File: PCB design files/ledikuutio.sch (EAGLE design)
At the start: 71 parts, among them IC1 ATMEGA328P, IC2 ISO7221A, IC3 74HC595D, Q2 MOSFET-NCHANNELSMD, Q3 16mhz, T1 TIP42, T2 TIP42, T3 TIP42, T4 TIP42, T5 TIP42, T6 TIP42, T7 TIP42, T8 TIP42, X1 2516-, X2 5566-20, X3 2516-, X4 2516-, X5 2516-, X6 2510-, X7 ANALOG IO

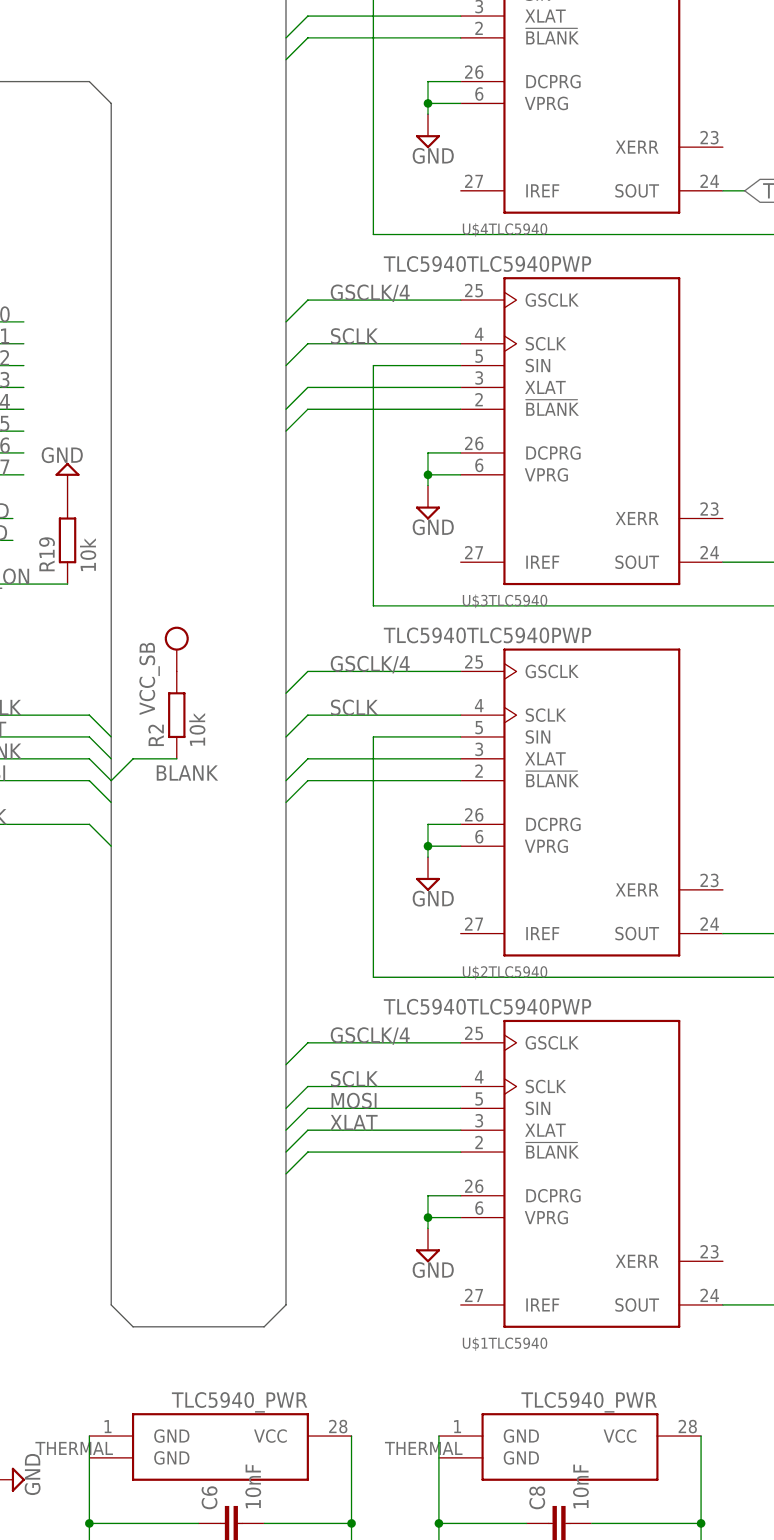
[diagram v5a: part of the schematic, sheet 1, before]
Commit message: Add missing IREF resistors.
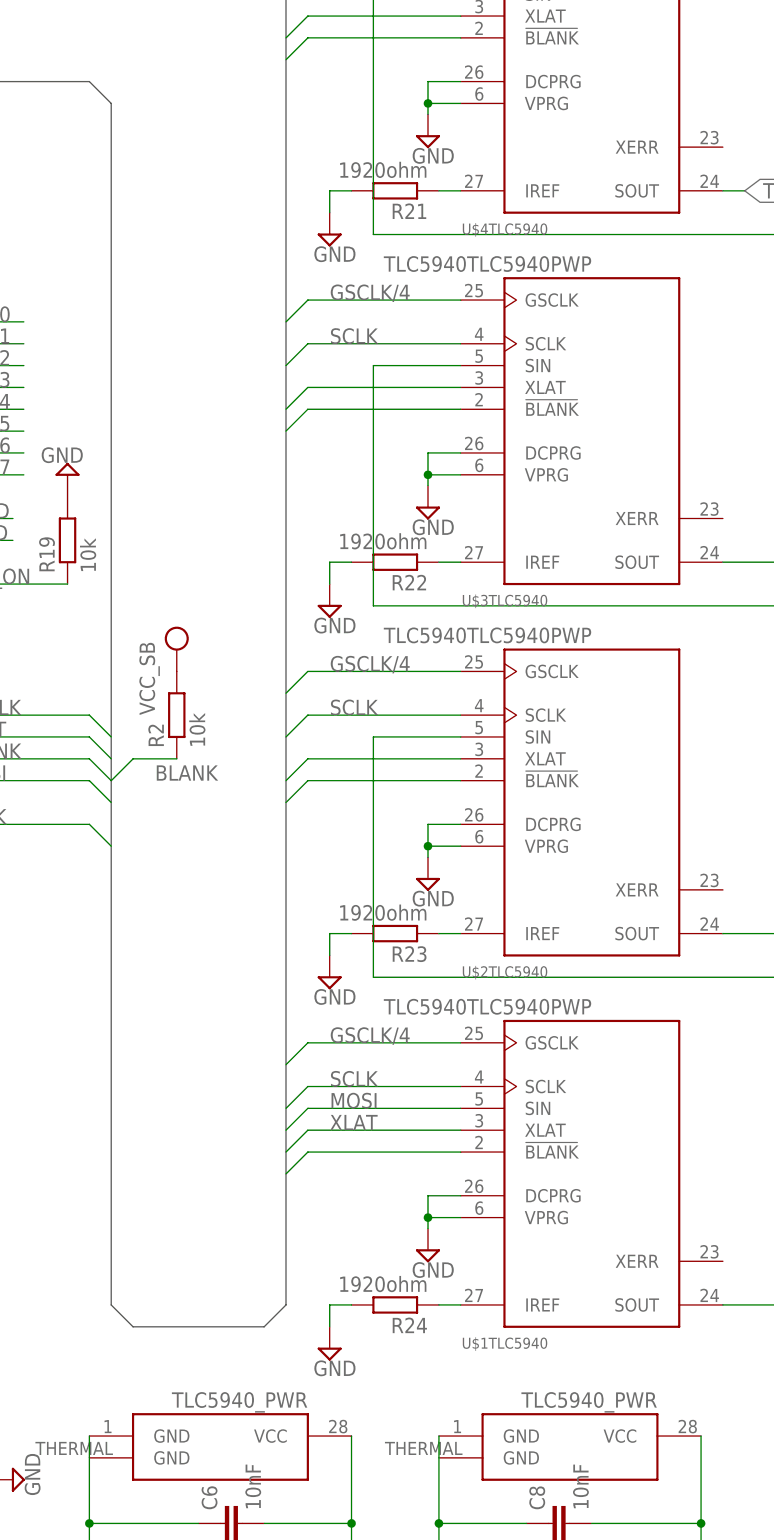
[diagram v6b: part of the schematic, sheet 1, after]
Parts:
- added R21, R22, R23, R24: 1920ohm, rcl:R-EU_M0805
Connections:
- new net N$48: R24.1, U$1TLC5940.IREF
- new net N$5: R21.1, U$4TLC5940.IREF
- new net N$6: R23.1, U$2TLC5940.IREF
- new net N$99: R22.1, U$3TLC5940.IREF
- net GND: now also R21.2, R22.2, R23.2, R24.2
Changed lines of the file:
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@@
 <part name="SUPPLY25" library="supply2" deviceset="GND" device=""/>
 <part name="R20" library="rcl" deviceset="R-EU_" device="M0805" value="10k"/>
+<part name="R21" library="rcl" deviceset="R-EU_" device="M0805" value="1920ohm"/>
+<part name="SUPPLY26" library="supply2" deviceset="GND" device=""/>
+<part name="R22" library="rcl" deviceset="R-EU_" device="M0805" value="1920ohm"/>
+<part name="R23" library="rcl" deviceset="R-EU_" device="M0805" value="1920ohm"/>
+<part name="R24" library="rcl" deviceset="R-EU_" device="M0805" value="1920ohm"/>
+<part name="SUPPLY27" library="supply2" deviceset="GND" device=""/>
+<part name="SUPPLY28" library="supply2" deviceset="GND" device=""/>
+<part name="SUPPLY29" library="supply2" deviceset="GND" device=""/>
 </parts>
 <sheets>
@@
 <instance part="SUPPLY25" gate="GND" x="20.32" y="203.2"/>
 <instance part="R20" gate="G$1" x="38.1" y="205.74" rot="R90"/>
+<instance part="R21" gate="G$1" x="149.86" y="213.36" rot="R180"/>
+<instance part="SUPPLY26" gate="GND" x="142.24" y="208.28"/>
+<instance part="R22" gate="G$1" x="149.86" y="170.18" rot="R180"/>
+<instance part="R23" gate="G$1" x="149.86" y="127" rot="R180"/>
+<instance part="R24" gate="G$1" x="149.86" y="83.82" rot="R180"/>
+<instance part="SUPPLY27" gate="GND" x="142.24" y="165.1"/>
+<instance part="SUPPLY28" gate="GND" x="142.24" y="121.92"/>
+<instance part="SUPPLY29" gate="GND" x="142.24" y="78.74"/>
 </instances>
 <busses>
@@
 <pinref part="SUPPLY25" gate="GND" pin="GND"/>
 </segment>
+<segment>
+<pinref part="SUPPLY26" gate="GND" pin="GND"/>
+<pinref part="R21" gate="G$1" pin="2"/>
+<wire x1="142.24" y1="210.82" x2="142.24" y2="213.36" width="0.1524" layer="91"/>
+<wire x1="142.24" y1="213.36" x2="144.78" y2="213.36" width="0.1524" layer="91"/>
+</segment>
+<segment>
+<pinref part="SUPPLY29" gate="GND" pin="GND"/>
+<pinref part="R24" gate="G$1" pin="2"/>
+<wire x1="142.24" y1="81.28" x2="142.24" y2="83.82" width="0.1524" layer="91"/>
+<wire x1="142.24" y1="83.82" x2="144.78" y2="83.82" width="0.1524" layer="91"/>
+</segment>
+<segment>
+<pinref part="SUPPLY28" gate="GND" pin="GND"/>
+<pinref part="R23" gate="G$1" pin="2"/>
+<wire x1="142.24" y1="124.46" x2="142.24" y2="127" width="0.1524" layer="91"/>
+<wire x1="142.24" y1="127" x2="144.78" y2="127" width="0.1524" layer="91"/>
+</segment>
+<segment>
+<pinref part="SUPPLY27" gate="GND" pin="GND"/>
+<pinref part="R22" gate="G$1" pin="2"/>
+<wire x1="142.24" y1="167.64" x2="142.24" y2="170.18" width="0.1524" layer="91"/>
+<wire x1="142.24" y1="170.18" x2="144.78" y2="170.18" width="0.1524" layer="91"/>
+</segment>
 </net>
 <net name="MOSI" class="1">
@@
 </segment>
 </net>
+<net name="N$5" class="0">
+<segment>
+<pinref part="R21" gate="G$1" pin="1"/>
+<pinref part="U$4" gate="TLC5940" pin="IREF"/>
+<wire x1="154.94" y1="213.36" x2="157.48" y2="213.36" width="0.1524" layer="91"/>
+</segment>
+</net>
+<net name="N$6" class="0">
+<segment>
+<pinref part="R23" gate="G$1" pin="1"/>
+<pinref part="U$2" gate="TLC5940" pin="IREF"/>
+<wire x1="154.94" y1="127" x2="157.48" y2="127" width="0.1524" layer="91"/>
+</segment>
+</net>
+<net name="N$48" class="0">
+<segment>
+<pinref part="R24" gate="G$1" pin="1"/>
+<pinref part="U$1" gate="TLC5940" pin="IREF"/>
+<wire x1="154.94" y1="83.82" x2="157.48" y2="83.82" width="0.1524" layer="91"/>
+</segment>
+</net>
+<net name="N$99" class="0">
+<segment>
+<pinref part="R22" gate="G$1" pin="1"/>
+<pinref part="U$3" gate="TLC5940" pin="IREF"/>
+<wire x1="154.94" y1="170.18" x2="157.48" y2="170.18" width="0.1524" layer="91"/>
+</segment>
+</net>

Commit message: Tweak drill sizes and add tip42C to local library.
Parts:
- T1, T2, T3, T4, T5, T6, T7, T8: device transistor-power:TIP42C -> elovalo:TIP42C
